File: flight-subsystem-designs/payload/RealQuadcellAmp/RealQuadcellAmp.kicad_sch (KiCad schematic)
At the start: 90 parts, among them J1 Screw_Terminal_01x02, J2 Conn_01x04_Pin, J3 Conn_01x04_Pin, U1 OPA1642AID, U2 OPA1642AID, U3 OPA1642AID, U4 OPA1642AID, U6 L78L33_SOT89

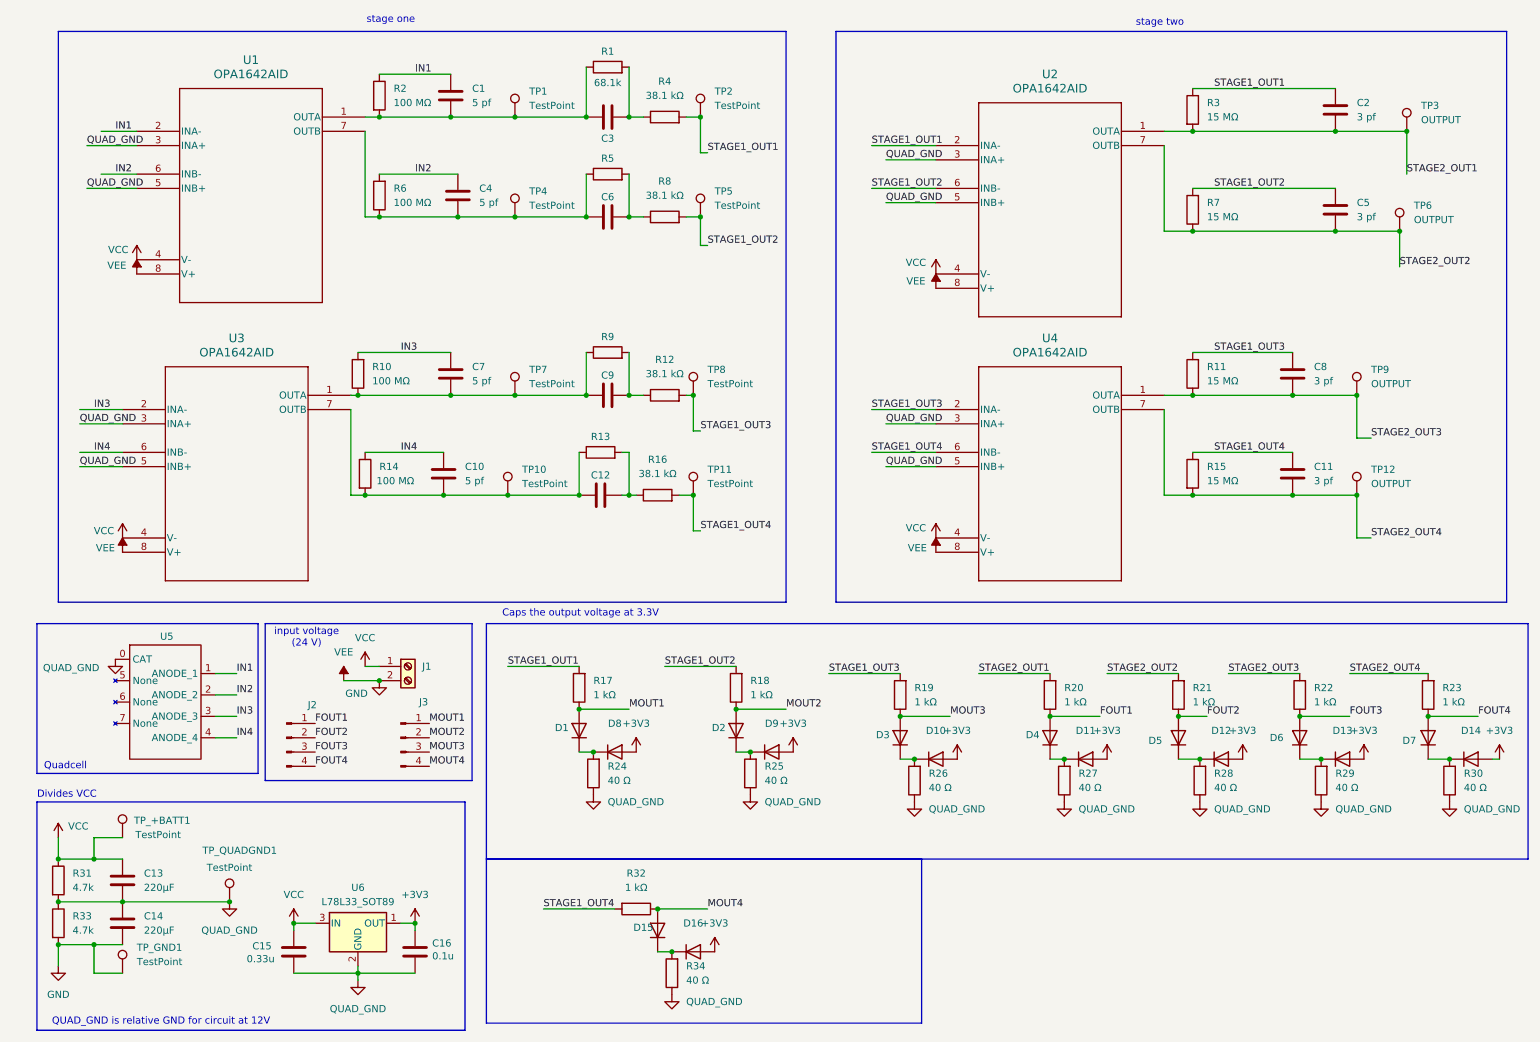
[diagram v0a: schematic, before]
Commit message: feat added new op amps and fied voltage divider problem on qc board
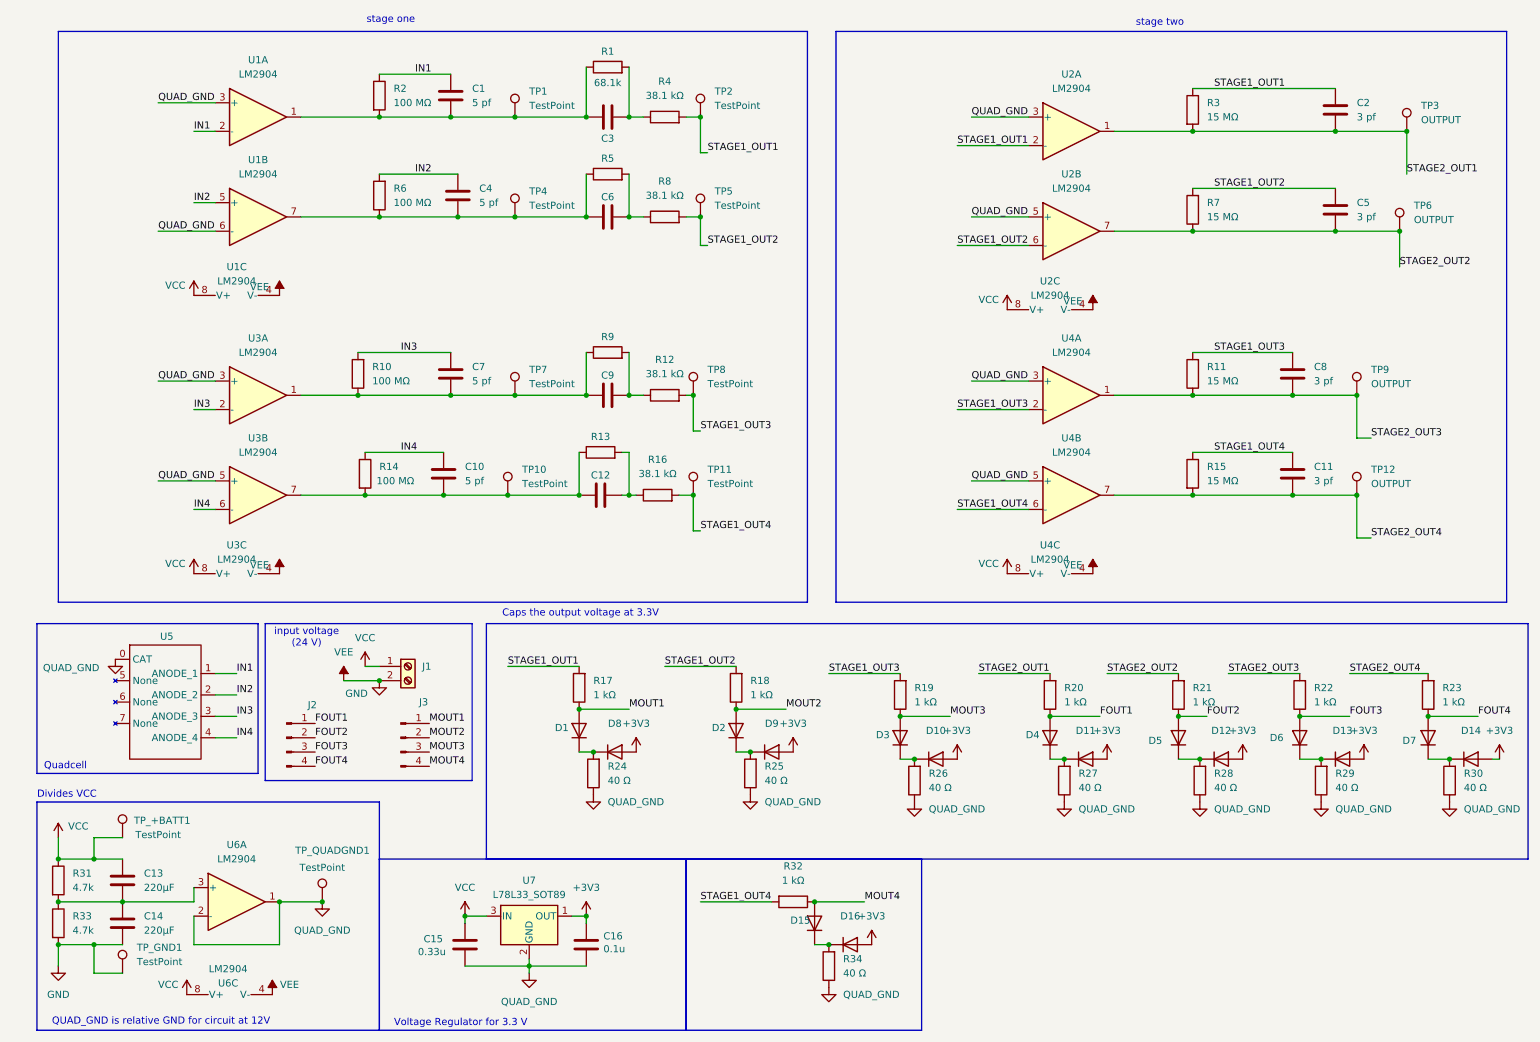
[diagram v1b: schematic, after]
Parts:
- removed U1, U2, U3, U4: OPA1642AID, OPA1642:D8, symbol OPA 1642:OPA1642AID
- removed U6: L78L33_SOT89, Package_TO_SOT_SMD:SOT-89-3, symbol Regulator_Linear:L78L33_SOT89
- added U1, U2, U3, U4, U6: LM2904, Package_SO:SOIC-8_3.9x4.9mm_P1.27mm, symbol Amplifier_Operational:LM2904
- added U7: L78L33_SOT89, Package_TO_SOT_SMD:SOT-89-3, symbol Regulator_Linear:L78L33_SOT89
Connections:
- net +3V3: now also U7.1 (OUT)
- net GND: now also U1.4 (V-), U2.4 (V-), U3.4 (V-), U4.4 (V-), U6.4 (V-)
- net IN1: now also U1.2 (-)
- net IN2: now also U1.5 (+)
- net IN3: now also U3.2 (-)
- net IN4: now also U3.6 (-)
- net QUAD_GND: now also U1.3 (+), U1.6 (-), U2.3 (+), U2.5 (+), U3.3 (+), U3.5 (+), U4.3 (+), U4.5 (+), U6.1, U6.2 (-), U7.2 (GND); no longer C13.2, C14.1, R31.2, R33.1
- net STAGE1_OUT1: now also U2.2 (-)
- net STAGE1_OUT2: now also U2.6 (-)
- net STAGE1_OUT3: now also U4.2 (-)
- net STAGE1_OUT4: now also U4.6 (-)
- net STAGE2_OUT1: now also U2.1
- net STAGE2_OUT2: now also U2.7
- net STAGE2_OUT3: now also U4.1
- net STAGE2_OUT4: now also U4.7
- net VCC: now also U1.8 (V+), U2.8 (V+), U3.8 (V+), U4.8 (V+), U6.8 (V+), U7.3 (IN)
- net at C4.2, C6.1, R5.1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: now also U1.7
- net at C10.2, C12.1, R13.1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: now also U3.7
- net at C7.2, C9.1, R10.1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: now also U3.1
- net at C1.2, C3.1, R1.1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: now also U1.1
- new net: C13.2, C14.1, R31.2, R33.1, U6.3 (+)
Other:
- note added: "Voltage Regulator for 3.3 V"
- moved on the sheet: D15, D16, R32, R34, TP_QUADGND1

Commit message: new quadcell rev
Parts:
- removed C15: 0.33u, Capacitor_SMD:C_0805_2012Metric_Pad1.18x1.45mm_HandSolder, symbol Device:C
- removed C16: 0.1u, Capacitor_SMD:C_0805_2012Metric_Pad1.18x1.45mm_HandSolder, symbol Device:C
- removed D1, D10, D11, D12, D13, D14, D15, D16, D2, D3, D4, D5, D6, D7, D8, D9: ~, Diode_SMD:D_0805_2012Metric_Pad1.15x1.40mm_HandSolder, symbol Diode:1N4001
- removed R17, R18, R19, R20, R21, R22, R23, R32: 1 kΩ, Resistor_SMD:R_0805_2012Metric_Pad1.20x1.40mm_HandSolder, symbol Device:R
- removed R24, R25, R26, R27, R28, R29, R30, R34: 40 Ω, Resistor_SMD:R_0805_2012Metric_Pad1.20x1.40mm_HandSolder, symbol Device:R
- removed U7: L78L33_SOT89, Package_TO_SOT_SMD:SOT-89-3, symbol Regulator_Linear:L78L33_SOT89
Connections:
- net FOUT1 is gone; now on net STAGE2_OUT1: J2.1 (Pin_1)
- net FOUT2 is gone; now on net STAGE2_OUT2: J2.2 (Pin_2)
- net FOUT3 is gone; now on net STAGE2_OUT3: J2.3 (Pin_3)
- net FOUT4 is gone; now on net STAGE2_OUT4: J2.4 (Pin_4)
- net MOUT1 is gone; now on net STAGE1_OUT1: J3.1 (Pin_1)
- net MOUT2 is gone; now on net STAGE1_OUT2: J3.2 (Pin_2)
- net MOUT3 is gone; now on net STAGE1_OUT3: J3.3 (Pin_3)
- net MOUT4 is gone; now on net STAGE1_OUT4: J3.4 (Pin_4)
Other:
- note removed: "Caps the output voltage at 3.3V"
- note removed: "Voltage Regulator for 3.3 V"
- moved on the sheet: C13, C14, J1, J2, J3, R31, R33, TP_+BATT1, TP_GND1, TP_QUADGND1, U5, U6A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

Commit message: qc amp changes
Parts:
- removed TP12, TP3, TP6, TP9: OUTPUT, TestPoint:TestPoint_Loop_D2.50mm_Drill1.0mm, symbol Connector:TestPoint
